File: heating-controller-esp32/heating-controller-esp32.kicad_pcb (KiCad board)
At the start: 2 copper layers, 103.3 x 146.8 mm, 123 parts, among them J1 431151015826, J11 USB_C_Receptacle_USB2.0, J2 431151015826, J3 76829-0104, J4 76829-0104, J5 76829-0104, J6 76829-0104, J7 76829-0104, J8 76829-0104, J9 76829-0104, Q1 MBT3904DW1, U1 ESP32-WROOM-32U, U10 MOC3061M, U2 CP2102N-A01-GQFN28, U4 MOC3061M, U6 MOC3061M, U7 MOC3061M, U8 MOC3061M, U9 MOC3061M

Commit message: Changes for JLCB fabrication using https://github.com/Bouni/kicad-jlcpcb-tools
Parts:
- D1, D10, D13, D20, D21, D5, D7, D8, D9: value ~ -> BAS-040
- R14, R26, R31, R32, R33, R34, R41, R50, R51: value ~ -> 4.7K
- R25: value ~ -> 5.1K
- U5: value ~ -> USB ESD
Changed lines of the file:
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@@
       (effects (font (size 1 1) (thickness 0.15)))
     )
-    (fp_text value "~" (at 0 2.4) (layer "F.Fab")
+    (fp_text value "BAS-040" (at 0 2.4) (layer "F.Fab")
       (effects (font (size 1 1) (thickness 0.15)))
     )
@@
       (effects (font (size 1 1) (thickness 0.15)))
     )
-    (fp_text value "~" (at 0 2.4) (layer "F.Fab")
+    (fp_text value "BAS-040" (at 0 2.4) (layer "F.Fab")
       (effects (font (size 1 1) (thickness 0.15)))
     )
@@
       (effects (font (size 1 1) (thickness 0.15)))
     )
-    (fp_text value "~" (at 0 1.43) (layer "F.Fab")
+    (fp_text value "4.7K" (at 0 1.43) (layer "F.Fab")
       (effects (font (size 1 1) (thickness 0.15)))
     )
@@
       (effects (font (size 1 1) (thickness 0.15)))
     )
-    (fp_text value "~" (at 0 2.4) (layer "F.Fab")
+    (fp_text value "BAS-040" (at 0 2.4) (layer "F.Fab")
       (effects (font (size 1 1) (thickness 0.15)))
     )
@@
       (effects (font (size 1 1) (thickness 0.15)))
     )
-    (fp_text value "~" (at 0 2.4) (layer "F.Fab")
+    (fp_text value "BAS-040" (at 0 2.4) (layer "F.Fab")
       (effects (font (size 1 1) (thickness 0.15)))
     )
@@
       (effects (font (size 1 1) (thickness 0.15)))
     )
-    (fp_text value "~" (at 0 1.43) (layer "F.Fab")
+    (fp_text value "4.7K" (at 0 1.43) (layer "F.Fab")
       (effects (font (size 1 1) (thickness 0.15)))
     )
@@
       (effects (font (size 1 1) (thickness 0.15)))
     )
-    (fp_text value "~" (at 0 1.43) (layer "F.Fab")
+    (fp_text value "4.7K" (at 0 1.43) (layer "F.Fab")
       (effects (font (size 1 1) (thickness 0.15)))
     )
@@
       (effects (font (size 1 1) (thickness 0.15)))
     )
-    (fp_text value "~" (at 0 1.43) (layer "F.Fab")
+    (fp_text value "4.7K" (at 0 1.43) (layer "F.Fab")
       (effects (font (size 1 1) (thickness 0.15)))
     )
@@
       (effects (font (size 1 1) (thickness 0.15)))
     )
-    (fp_text value "~" (at 0 1.43) (layer "F.Fab")
+    (fp_text value "4.7K" (at 0 1.43) (layer "F.Fab")
       (effects (font (size 1 1) (thickness 0.15)))
     )
@@
       (effects (font (size 1 1) (thickness 0.15)))
     )
-    (fp_text value "~" (at 0 2.4) (layer "F.Fab")
+    (fp_text value "BAS-040" (at 0 2.4) (layer "F.Fab")
       (effects (font (size 1 1) (thickness 0.15)))
     )
@@
       (effects (font (size 1 1) (thickness 0.15)))
     )
-    (fp_text value "~" (at 0 2.4) (layer "F.Fab")
+    (fp_text value "BAS-040" (at 0 2.4) (layer "F.Fab")
       (effects (font (size 1 1) (thickness 0.15)))
     )
@@
       (effects (font (size 1 1) (thickness 0.15)))
     )
-    (fp_text value "~" (at 0 1.43) (layer "F.Fab")
+    (fp_text value "4.7K" (at 0 1.43) (layer "F.Fab")
       (effects (font (size 1 1) (thickness 0.15)))
     )
@@
       (effects (font (size 1 1) (thickness 0.15)))
     )
-    (fp_text value "~" (at 0 1.43) (layer "F.Fab")
+    (fp_text value "5.1K" (at 0 1.43) (layer "F.Fab")
       (effects (font (size 1 1) (thickness 0.15)))
     )
@@
       (effects (font (size 1 1) (thickness 0.15)))
     )
-    (fp_text value "~" (at 0 2.4) (layer "F.Fab")
+    (fp_text value "BAS-040" (at 0 2.4) (layer "F.Fab")
       (effects (font (size 1 1) (thickness 0.15)))
     )
@@
       (effects (font (size 1 1) (thickness 0.15)))
     )
-    (fp_text value "~" (at 0 1.43) (layer "F.Fab")
+    (fp_text value "4.7K" (at 0 1.43) (layer "F.Fab")
       (effects (font (size 1 1) (thickness 0.15)))
     )
@@
       (effects (font (size 1 1) (thickness 0.15)))
     )
-    (fp_text value "~" (at 0 2.4) (layer "F.Fab")
+    (fp_text value "BAS-040" (at 0 2.4) (layer "F.Fab")
       (effects (font (size 1 1) (thickness 0.15)))
     )
@@
       (effects (font (size 1 1) (thickness 0.15)))
     )
-    (fp_text value "~" (at 0 1.75) (layer "F.Fab")
+    (fp_text value "USB ESD" (at 0 1.75) (layer "F.Fab")
       (effects (font (size 1 1) (thickness 0.15)))
     )
@@
       (effects (font (size 1 1) (thickness 0.15)))
     )
-    (fp_text value "~" (at 0 2.4) (layer "F.Fab")
+    (fp_text value "BAS-040" (at 0 2.4) (layer "F.Fab")
       (effects (font (size 1 1) (thickness 0.15)))
     )
@@
       (effects (font (size 1 1) (thickness 0.15)))
     )
-    (fp_text value "~" (at 0 1.43) (layer "F.Fab")
+    (fp_text value "4.7K" (at 0 1.43) (layer "F.Fab")
       (effects (font (size 1 1) (thickness 0.15)))
     )
@@
       (effects (font (size 1 1) (thickness 0.15)))
     )
-    (fp_text value "~" (at 0 1.43) (layer "F.Fab")
+    (fp_text value "4.7K" (at 0 1.43) (layer "F.Fab")
       (effects (font (size 1 1) (thickness 0.15)))
     )

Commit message: Minor updates and update of README.md
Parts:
- R16, R19, R22, R29, R36, R39: value 360R -> 330R
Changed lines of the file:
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@@
     (descr "Resistor SMD 0603 (1608 Metric), square (rectangular) end terminal, IPC_7351 nominal, (Body size source: IPC-SM-782 page 72, https://www.pcb-3d.com/wordpress/wp-content/uploads/ipc-sm-782a_amendment_1_and_2.pdf), generated with kicad-footprint-generator")
     (tags "resistor")
-    (property "LCSC" "C25194")
+    (property "LCSC" "C23138")
     (property "Sheetfile" "ssr.kicad_sch")
     (property "Sheetname" "Pump Out")
@@
       (effects (font (size 1 1) (thickness 0.15)))
     )
-    (fp_text value "360R" (at 0 1.43 90) (layer "F.Fab")
+    (fp_text value "330R" (at 0 1.43 90) (layer "F.Fab")
       (effects (font (size 1 1) (thickness 0.15)))
     )
@@
     (descr "Resistor SMD 0603 (1608 Metric), square (rectangular) end terminal, IPC_7351 nominal, (Body size source: IPC-SM-782 page 72, https://www.pcb-3d.com/wordpress/wp-content/uploads/ipc-sm-782a_amendment_1_and_2.pdf), generated with kicad-footprint-generator")
     (tags "resistor")
-    (property "LCSC" "C25194")
+    (property "LCSC" "C23138")
     (property "Sheetfile" "ssr.kicad_sch")
     (property "Sheetname" "Boiler Out")
@@
       (effects (font (size 1 1) (thickness 0.15)))
     )
-    (fp_text value "360R" (at 0 1.43 90) (layer "F.Fab")
+    (fp_text value "330R" (at 0 1.43 90) (layer "F.Fab")
       (effects (font (size 1 1) (thickness 0.15)))
     )
@@
     (descr "Resistor SMD 0603 (1608 Metric), square (rectangular) end terminal, IPC_7351 nominal, (Body size source: IPC-SM-782 page 72, https://www.pcb-3d.com/wordpress/wp-content/uploads/ipc-sm-782a_amendment_1_and_2.pdf), generated with kicad-footprint-generator")
     (tags "resistor")
-    (property "LCSC" "C25194")
+    (property "LCSC" "C23138")
     (property "Sheetfile" "ssr.kicad_sch")
     (property "Sheetname" "Valve Out 4")
@@
       (effects (font (size 1 1) (thickness 0.15)))
     )
-    (fp_text value "360R" (at 0 1.43 90) (layer "F.Fab")
+    (fp_text value "330R" (at 0 1.43 90) (layer "F.Fab")
       (effects (font (size 1 1) (thickness 0.15)))
     )
@@
     (descr "Resistor SMD 0603 (1608 Metric), square (rectangular) end terminal, IPC_7351 nominal, (Body size source: IPC-SM-782 page 72, https://www.pcb-3d.com/wordpress/wp-content/uploads/ipc-sm-782a_amendment_1_and_2.pdf), generated with kicad-footprint-generator")
     (tags "resistor")
-    (property "LCSC" "C25194")
+    (property "LCSC" "C23138")
     (property "Sheetfile" "ssr.kicad_sch")
     (property "Sheetname" "Valve Out 2")
@@
       (effects (font (size 1 1) (thickness 0.15)))
     )
-    (fp_text value "360R" (at 0 1.43 90) (layer "F.Fab")
+    (fp_text value "330R" (at 0 1.43 90) (layer "F.Fab")
       (effects (font (size 1 1) (thickness 0.15)))
     )
@@
     (descr "Resistor SMD 0603 (1608 Metric), square (rectangular) end terminal, IPC_7351 nominal, (Body size source: IPC-SM-782 page 72, https://www.pcb-3d.com/wordpress/wp-content/uploads/ipc-sm-782a_amendment_1_and_2.pdf), generated with kicad-footprint-generator")
     (tags "resistor")
-    (property "LCSC" "C25194")
+    (property "LCSC" "C23138")
     (property "Sheetfile" "ssr.kicad_sch")
     (property "Sheetname" "Valve Out 3")
@@
       (effects (font (size 1 1) (thickness 0.15)))
     )
-    (fp_text value "360R" (at 0 1.43 90) (layer "F.Fab")
+    (fp_text value "330R" (at 0 1.43 90) (layer "F.Fab")
       (effects (font (size 1 1) (thickness 0.15)))
     )
@@
     (descr "Resistor SMD 0603 (1608 Metric), square (rectangular) end terminal, IPC_7351 nominal, (Body size source: IPC-SM-782 page 72, https://www.pcb-3d.com/wordpress/wp-content/uploads/ipc-sm-782a_amendment_1_and_2.pdf), generated with kicad-footprint-generator")
     (tags "resistor")
-    (property "LCSC" "C25194")
+    (property "LCSC" "C23138")
     (property "Sheetfile" "ssr.kicad_sch")
     (property "Sheetname" "Valve Out 1")
@@
       (effects (font (size 1 1) (thickness 0.15)))
     )
-    (fp_text value "360R" (at 0 1.43 90) (layer "F.Fab")
+    (fp_text value "330R" (at 0 1.43 90) (layer "F.Fab")
       (effects (font (size 1 1) (thickness 0.15)))
     )

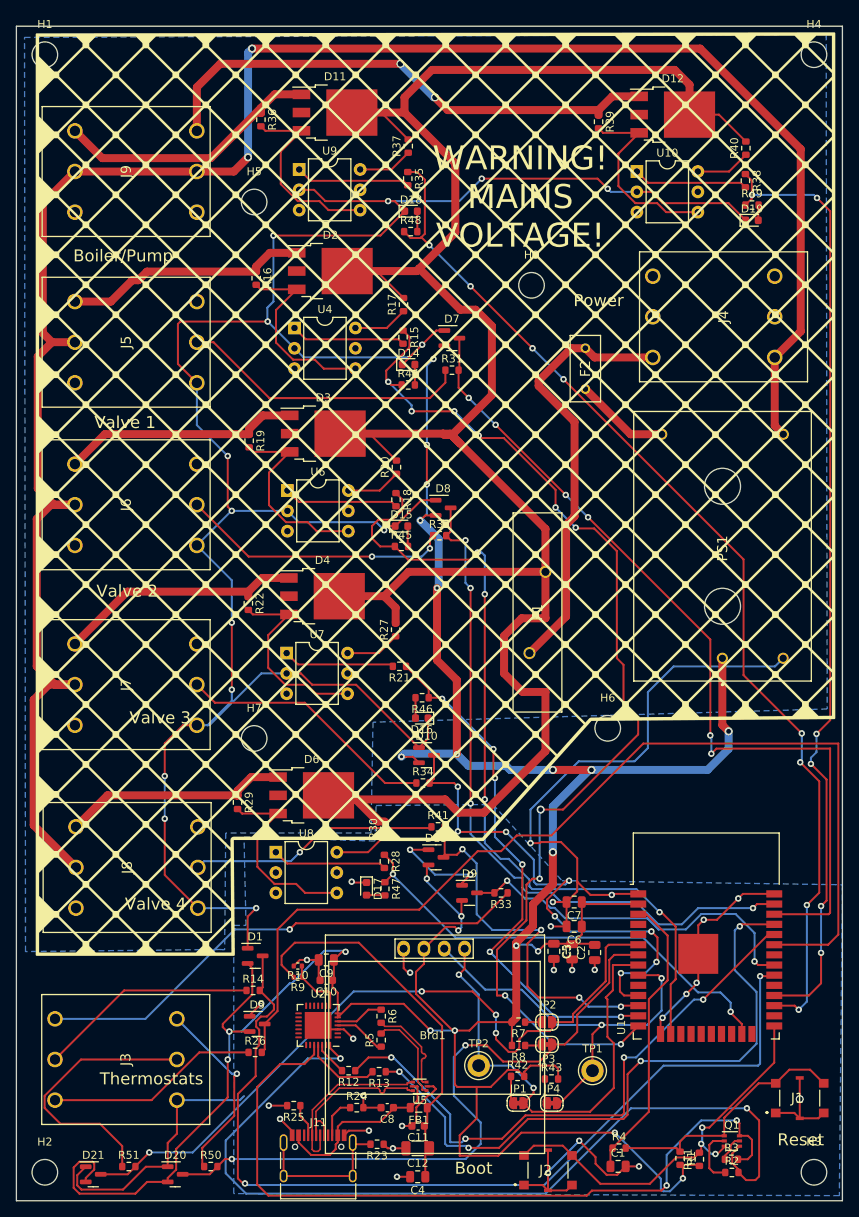
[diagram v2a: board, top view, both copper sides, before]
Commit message: Current limiting resistors for MOC devices changed to 0.5W
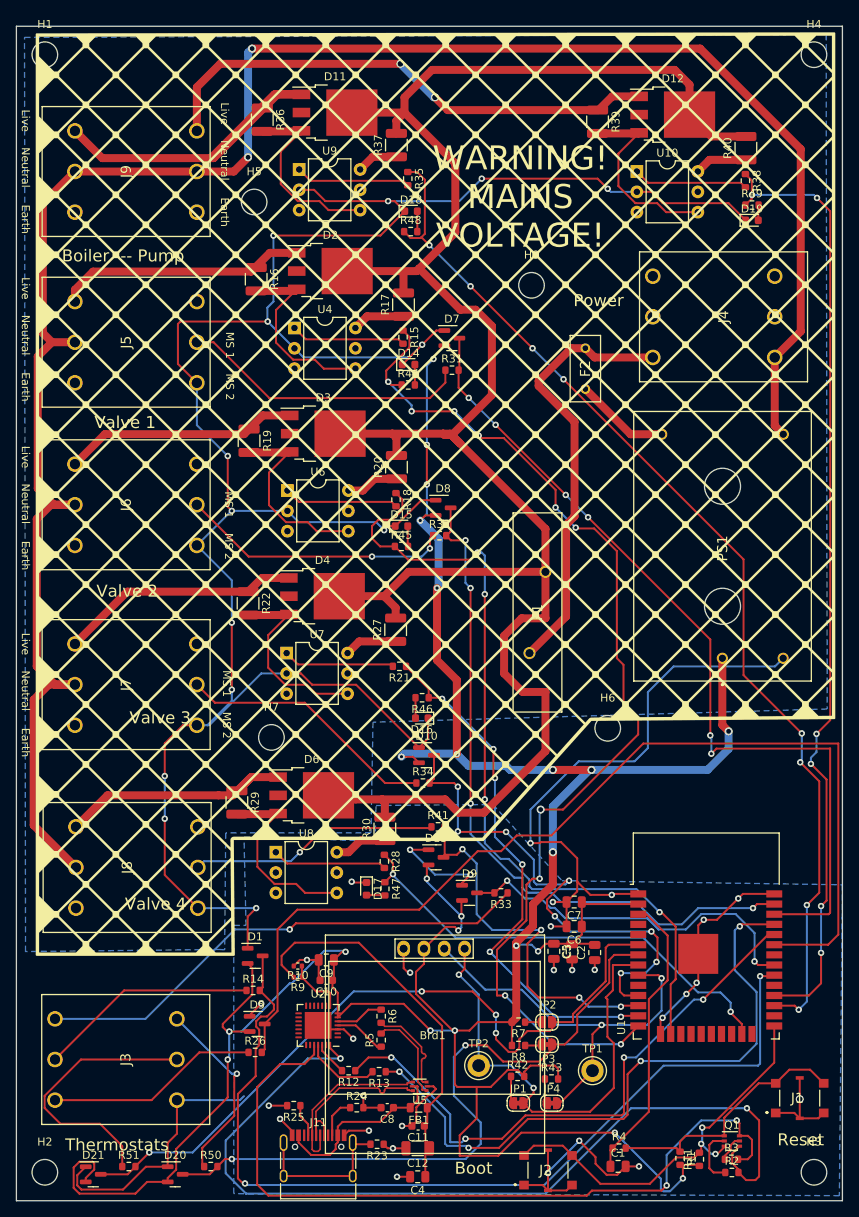
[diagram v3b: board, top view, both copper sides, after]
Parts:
- R16, R19, R22, R29, R36, R39: value 330R -> 360R; footprint Resistor_SMD:R_0603_1608Metric -> Resistor_SMD:R_1210_3225Metric
- R17, R20, R27, R30, R37, R40: footprint Resistor_SMD:R_0603_1608Metric -> Resistor_SMD:R_1210_3225Metric
- moved H7 2.16 mm to (41.8, 117.1)
- moved R37 1.49 mm to (57.4, 43.1)
- moved R36 0.17 mm to (40.6, 39.9)
- moved R39 0.13 mm to (82.5, 40.1)
- moved R16 0.13 mm to (39.9, 59.8)
- moved R29 0.08 mm to (37.5, 125.2)
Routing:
- net LINE: track 289.7 -> 265.0 mm
- net /Boiler Out/Switched: track 33.8 -> 52.3 mm
- net Net-(D12-Pad3): track 24.3 -> 28.7 mm
- net Net-(D6-Pad3): track 24.3 -> 28.7 mm
- net Net-(D2-Pad3): track 24.3 -> 28.7 mm
- net Net-(D4-Pad3): track 24.3 -> 28.6 mm
- net Net-(D3-Pad3): track 24.3 -> 28.6 mm
- net Net-(D11-Pad3): track 24.3 -> 28.4 mm
- net /Valve Out 4/Switched: track 28.2 -> 30.3 mm
- net Net-(R37-Pad1): track 6.88 -> 5.19 mm
- net /Valve Out 3/Switched: track 30.8 -> 30.2 mm
- net /Pump Out/Switched: track 65.7 -> 65.1 mm
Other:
- board text added: "Boiler --- Pump"
- board text added: "Earth"
- board text added: "Live"
- board text added: "MS 1"
- board text added: "MS 2"
- board text added: "Neutral"
- board text removed: "Boiler/Pump"

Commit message: Assign netclasses (should have done this earlier)! Small tweaks; status LED added.
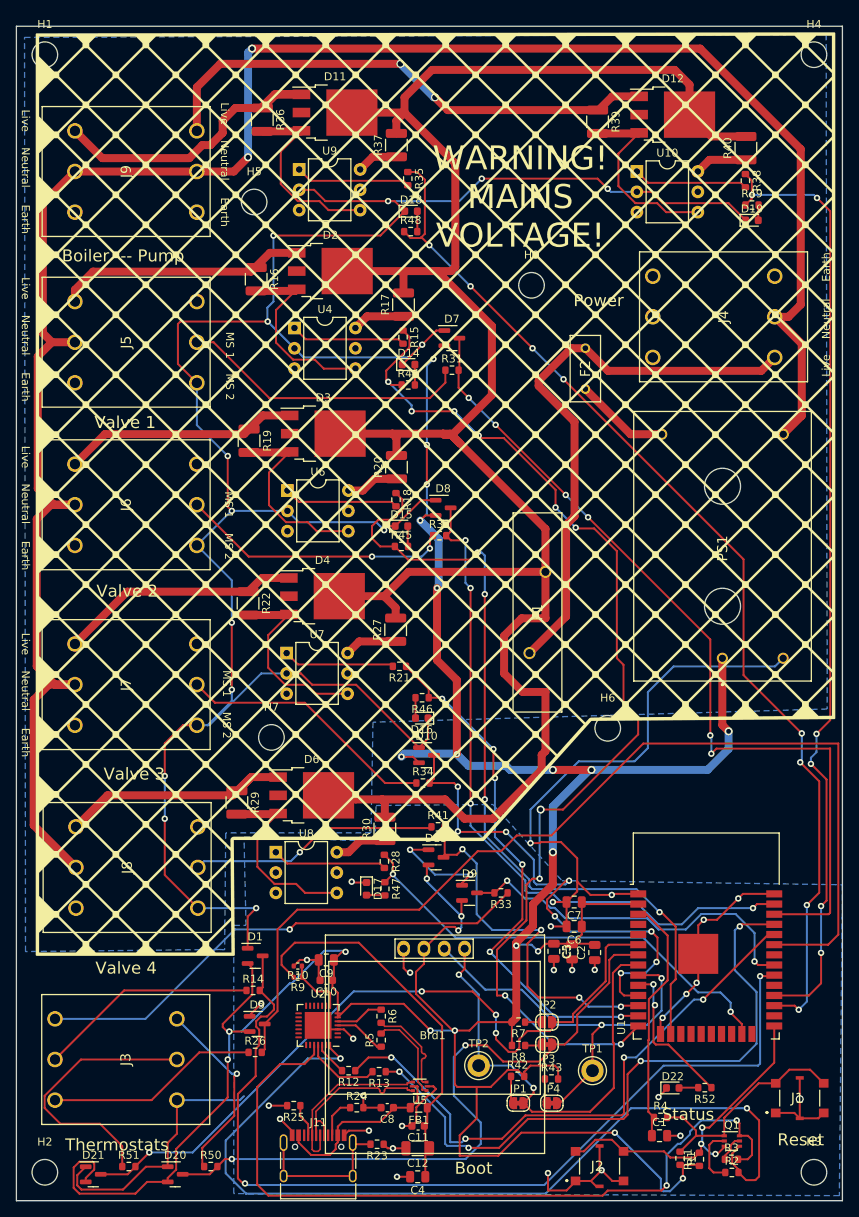
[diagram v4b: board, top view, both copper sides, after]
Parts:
- added D22: RED, LED_SMD:LED_0603_1608Metric, F.Cu at (91.9, 160.9)
- added R52: 1K, Resistor_SMD:R_0603_1608Metric, F.Cu at (96.0, 160.9)
- moved J2 6.47 mm to (82.8, 170.7)
- moved C1 6.45 mm to (90.3, 166.9)
- moved R4 6.45 mm to (90.4, 164.6)
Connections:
- J4 pad 1: NEUT -> Net-(F1-Pad1)
- J4 pad 2: Net-(F1-Pad1) -> unconnected-(J4-Pad2)
- J4 pad 3: Earth -> NEUT
- J4 pad 5: unconnected-(J4-Pad5) -> Earth
- U1 pad 10: /ESP32/IO25 -> /STATUS_LED
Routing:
- net /STATUS_LED: track 0.00 -> 18.9 mm, vias 0 -> 2
- net Net-(F1-Pad1): track 54.7 -> 71.3 mm
- net /Boiler Out/Switched: track 52.3 -> 39.7 mm
- net /ESP32/GPIO_0: track 50.2 -> 41.4 mm
- net GND: track 531.0 -> 523.9 mm, vias 44 -> 45
- net /ESP32/EN: track 36.6 -> 31.2 mm
- net NEUT: track 257.0 -> 259.9 mm
- net /ESP32/~{RESET}: track 32.0 -> 29.3 mm
- net Net-(D22-Pad2): track 0.00 -> 2.41 mm
- net LINE: track 265.0 -> 263.5 mm
- net /ESP32/IO32: track 58.7 -> 57.4 mm
- net /ESP32/IO13: track 102.6 -> 102.0 mm
- net /ESP32/IO23: track 87.8 -> 87.2 mm
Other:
- board text added: "Status"
